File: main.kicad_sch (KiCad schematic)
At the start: 84 parts, among them J1 USB_C_Receptacle, J2 Bus_M.2_Socket_M, U2 SPI_SOIC-8, U3 SPI_DFN-8, Y1 25MHz

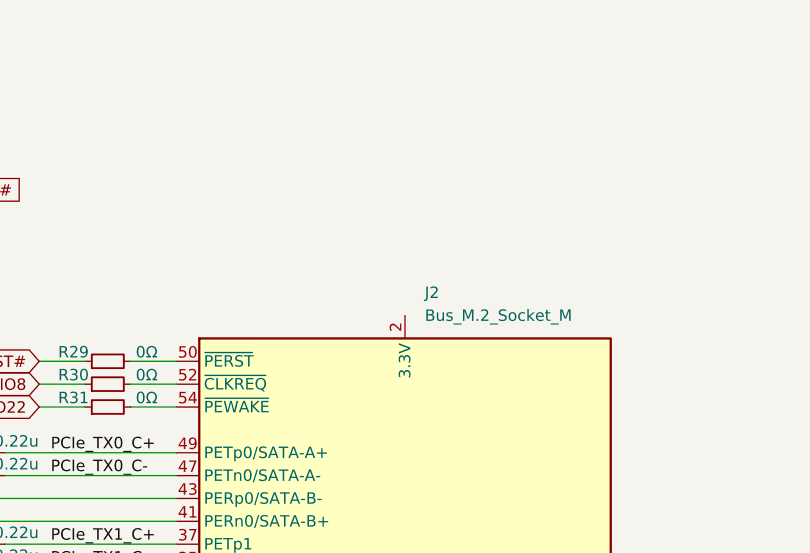
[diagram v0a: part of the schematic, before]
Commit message: Updated power rails
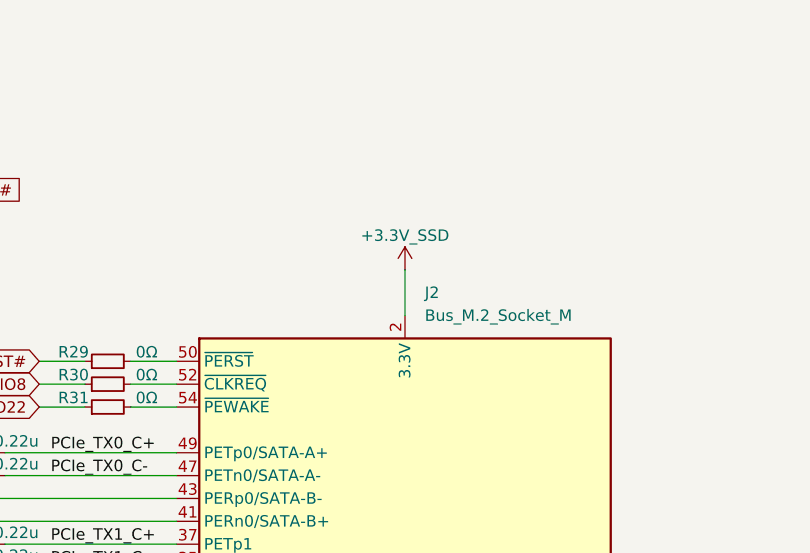
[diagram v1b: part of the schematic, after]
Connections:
- net +3.3V_SSD: now reaches J2.12 (3.3V), J2.14 (3.3V), J2.16 (3.3V), J2.18 (3.3V), J2.2 (3.3V), J2.4 (3.3V), J2.70 (3.3V), J2.72 (3.3V), J2.74 (3.3V)
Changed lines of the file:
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@@
 	(wire
 		(pts
+			(xy 481.33 55.88) (xy 481.33 60.96)
+		)
+		(stroke
+			(width 0)
+			(type default)
+		)
+	)
+	(wire
+		(pts
 			(xy 217.17 167.64) (xy 217.17 170.18)
 		)
@@
 				)
 			)
+		)
+	)
+	(symbol
+		(lib_id "power:+3.3V")
+		(at 481.33 55.88 0)
+		(unit 1)
+		(exclude_from_sim no)
+		(in_bom yes)
+		(on_board yes)
+		(dnp no)
+		(property "Reference" "#PWR041"
+			(at 481.33 59.69 0)
+			(effects
+				(font
+					(size 1.27 1.27)
+				)
+				(hide yes)
+			)
+		)
+		(property "Value" "+3.3V_SSD"
+			(at 481.33 52.07 0)
+			(effects
+				(font
+					(size 1.27 1.27)
+				)
+			)
+		)
+		(property "Footprint" ""
+			(at 481.33 55.88 0)
+			(effects
+				(font
+					(size 1.27 1.27)
+				)
+				(hide yes)
+			)
+		)
+		(property "Datasheet" ""
+			(at 481.33 55.88 0)
+			(effects
+				(font
+					(size 1.27 1.27)
+				)
+				(hide yes)
+			)
+		)
+		(property "Description" "Power symbol creates a global label with name \"+3.3V\""
+			(at 481.33 55.88 0)
+			(effects
+				(font
+					(size 1.27 1.27)
+				)
+				(hide yes)
+			)
+		)
+		(pin "1"
+		)
+		(instances
+			(project "ASM2464PD-test"
+				(path "/b2a945ac-f788-482b-9831-47d865c602eb/12c26485-ec0e-483e-81eb-3c9eea5d2424"
+					(reference "#PWR041")
+					(unit 1)
+				)
+			)

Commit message: Added todo list
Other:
- note added: "TODO: [ ] UART header 3V3 GND TX RX [ ] I2C header 3V3 GND CLK DATA [ ] SPI header with SPI flash pinout [ ] Jumper/button for SPI /HOLD [ ] Jumper/button for ASM RST#"
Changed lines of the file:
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@@
+		)
+	)
+	(text "TODO:\n[ ] UART header 3V3 GND TX RX\n[ ] I2C header 3V3 GND CLK DATA\n[ ] SPI header with SPI flash pinout\n[ ] Jumper/button for SPI /HOLD\n[ ] Jumper/button for ASM RST#"
+		(exclude_from_sim no)
+		(at 411.48 278.13 0)
+		(effects
+			(font
+				(size 1.27 1.27)
+			)
+			(justify left)
 		)
 	)

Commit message: Changing from M.2 adapter to PCIe x4 adapter
I don't actually want an ssd enclosure, I want a PCIe-slot-giver for my laptop
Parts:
- removed J2: Bus_M.2_Socket_M, A_my_stuff:m-key, symbol Connector:Bus_M.2_Socket_M
- removed R29: 0Ω, Resistor_SMD:R_0201_0603Metric, symbol Device:R_Small
- added J3: Bus_PCI_Express_x4, A-my-stuff:PCIe_x4_tht_open, symbol Connector:Bus_PCI_Express_x4
- C10, C11, C20, C21: footprint Capacitor_SMD:C_0201_0603Metric -> Capacitor_SMD:C_0402_1005Metric
- D1, D2: footprint (none) -> LED_SMD:LED_0603_1608Metric
- TP1, TP10, TP11, TP2, TP3, TP4, TP5, TP6, TP7, TP8, TP9: footprint (none) -> TestPoint:TestPoint_Pad_D2.0mm
- U1: footprint A_my_stuff:ASM2464PD -> A-my-stuff:ASM2464PD
- U2: footprint Package_SO:SOIC-8_5.23x5.23mm_P1.27mm -> Package_SO:SOIC-8_5.3x5.3mm_P1.27mm
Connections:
- net +3.3V_SSD: now also J3.A10 (+3.3V), J3.A9 (+3.3V), J3.B10 (3.3Vaux), J3.B8 (+3.3V)
- net GND: now also J3.A1 (~{PRSNT1}), J3.A12 (GND), J3.A15 (GND), J3.A18 (GND), J3.A20 (GND), J3.A23 (GND), J3.A24 (GND), J3.A27 (GND), J3.A28 (GND), J3.A31 (GND), J3.A4 (GND), J3.B13 (GND), J3.B16 (GND), J3.B18 (GND), J3.B21 (GND), J3.B22 (GND), J3.B25 (GND), J3.B26 (GND), J3.B29 (GND), J3.B32 (GND), J3.B4 (GND), J3.B7 (GND)
- net PCIe_RX0+: now also J3.A16 (PERp0)
- net PCIe_RX0-: now also J3.A17 (PERn0)
- net PCIe_RX1+: now also J3.A21 (PERp1)
- net PCIe_RX1-: now also J3.A22 (PERn1)
- net PCIe_RX2+: now also J3.A25 (PERp2)
- net PCIe_RX2-: now also J3.A26 (PERn2)
- net PCIe_RX3+: now also J3.A29 (PERp3)
- net PCIe_RX3-: now also J3.A30 (PERn3)
- net PCIe_TX0_C+: now also J3.B14 (PETp0)
- net PCIe_TX0_C-: now also J3.B15 (PETn0)
- net PCIe_TX1_C+: now also J3.B19 (PETp1)
- net PCIe_TX1_C-: now also J3.B20 (PETn1)
- net PCIe_TX2_C+: now also J3.B23 (PETp2)
- net PCIe_TX2_C-: now also J3.B24 (PETn2)
- net PCIe_TX3_C+: now also J3.B27 (PETp3)
- net PCIe_TX3_C-: now also J3.B28 (PETn3)
- net PERST#: now also J3.A11 (~{PERST})
- net REFCLK+: now also J3.A13 (REFCLK+)
- net REFCLK-: now also J3.A14 (REFCLK-)
- net at R31.2: now also J3.B11 (~{WAKE})
- net at R30.2: now also J3.B17 (~{PRSNT2}), J3.B31 (~{PRSNT2})
- new net: J3.A2 (+12V), J3.A3 (+12V), J3.B1 (+12V), J3.B2 (+12V), J3.B3 (+12V)
- no-connect marks 2 -> 0
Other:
- moved on the sheet: C12, C13, C14, C15, C16, C17, C18, C19, R30, R31

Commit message: Cleaning up schematic a bit
Directly copying the reference schematic was stupid lol, what a mess
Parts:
- removed unit 6 of U1
- removed unit 3 of U1
- removed unit 4 of U1
- removed unit 5 of U1
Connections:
- net GND: now also C21.1, R36.1, R37.1, R38.1; no longer C21.2, R36.2, R37.2, R38.2
- net RST#: now also C21.2; no longer C21.1
- net SPI_DO: now also R37.2; no longer R37.1
- net TEST_EN: now also R38.2; no longer R38.1
- net UART_TX: now also R36.2; no longer R36.1
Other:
- note added: "TODO: [ ] UART header 3V3 GND TX RX [ ] I2C header 3V3 GND CLK DATA [ ] SPI header with SPI flash pinout [ ] Jumper/button for SPI /HOLD [ ] Jumper/button for ASM RST# [ ] CC testpoints"
- note removed: "TODO: [ ] UART header 3V3 GND TX RX [ ] I2C header 3V3 GND CLK DATA [ ] SPI header with SPI flash pinout [ ] Jumper/button for SPI /HOLD [ ] Jumper/button for ASM RST#"
- moved on the sheet: C1, C10, C11, C12, C13, C14, C15, C16, C17, C18, C19, C2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

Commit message: power notes
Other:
- title: (none) -> ASM2464PD USB, PCIe, SPI & GPIO
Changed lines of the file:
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@@
 	(generator_version "9.0")
 	(paper "A3")
+	(title_block
+		(title "ASM2464PD USB, PCIe, SPI & GPIO")
+	)
 	(rectangle
 		(start 67.31 209.55)

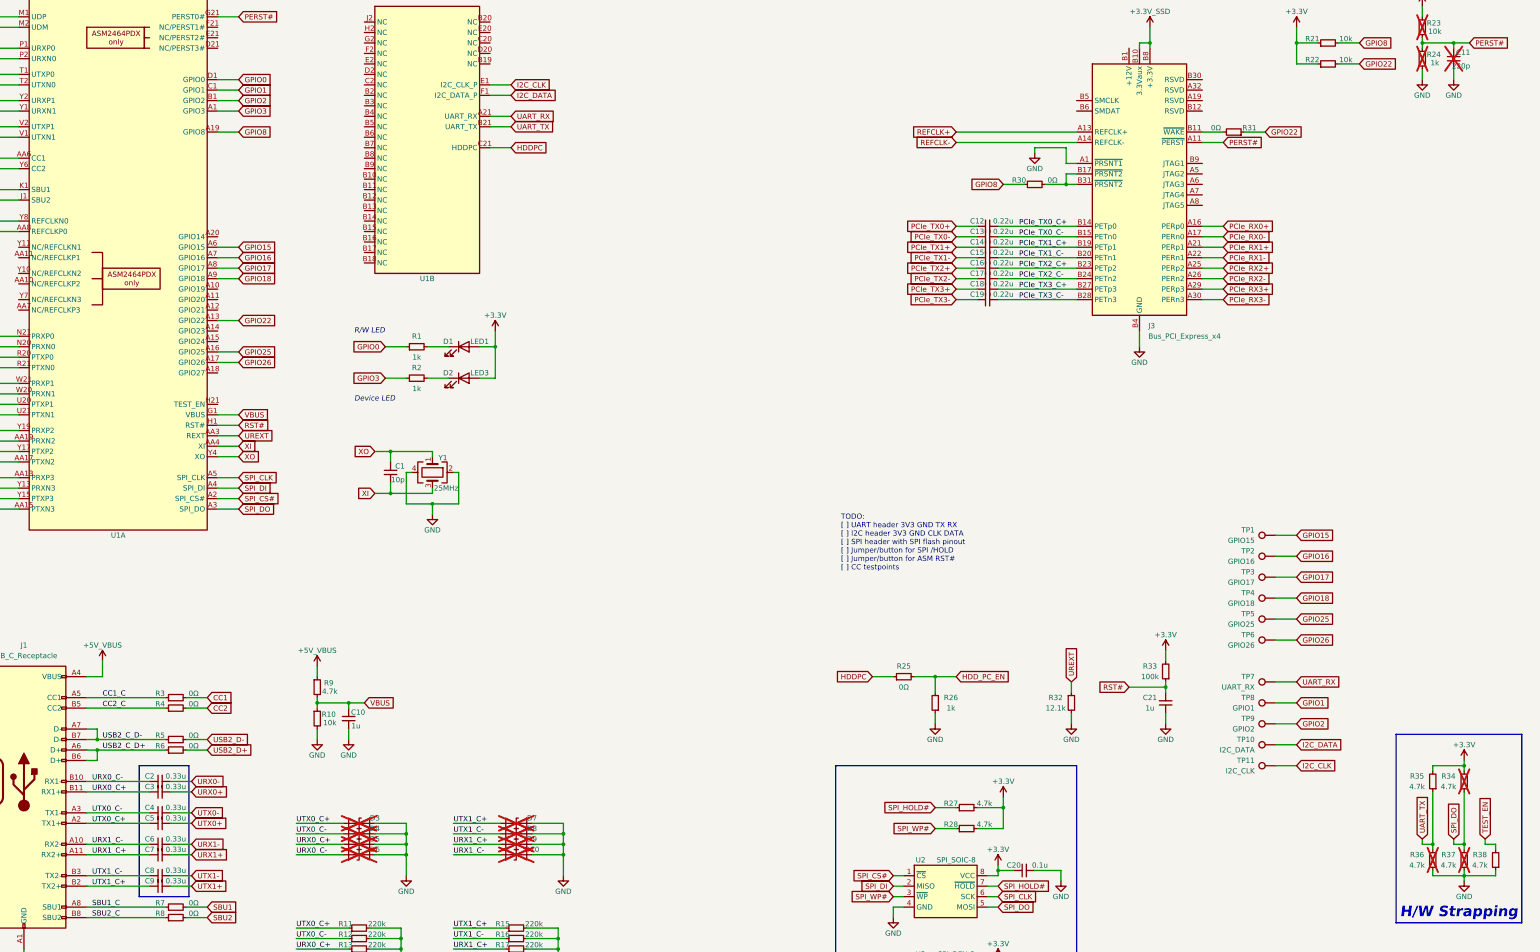
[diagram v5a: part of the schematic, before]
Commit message: Added function names to gpio pins
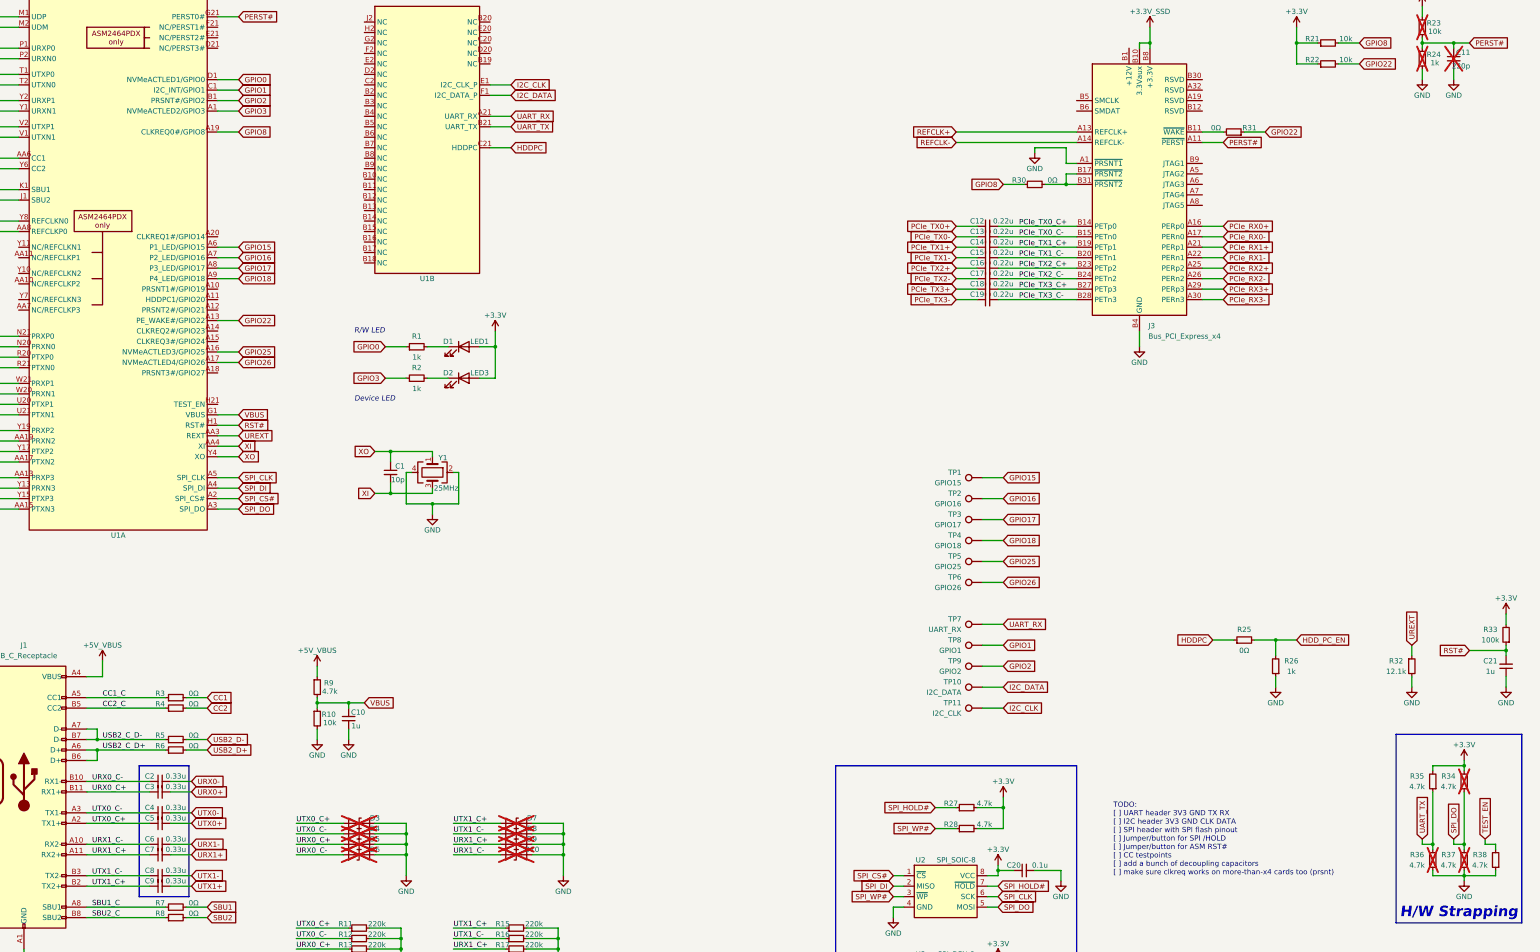
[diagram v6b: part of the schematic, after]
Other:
- note added: "TODO: [ ] UART header 3V3 GND TX RX [ ] I2C header 3V3 GND CLK DATA [ ] SPI header with SPI flash pinout [ ] Jumper/button for SPI /HOLD [ ] Jumper/button for ASM RST# [ ] CC testpoints [ ] add a bunch of decoupling capacitors [ ] make sure clkreq works on more-than-x4 cards too (prsnt)"
- note removed: "TODO: [ ] UART header 3V3 GND TX RX [ ] I2C header 3V3 GND CLK DATA [ ] SPI header with SPI flash pinout [ ] Jumper/button for SPI /HOLD [ ] Jumper/button for ASM RST# [ ] CC testpoints"
- moved on the sheet: C21, R25, R26, R32, R33, TP1, TP10, TP11, TP2, TP3, TP4, TP5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

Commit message: more pin names, more schematic cleanup, added SPI header
baby I don't know when I'm supposed to stop (I should go to bed)
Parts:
- removed TP1: GPIO15, TestPoint:TestPoint_Pad_D2.0mm, symbol Connector:TestPoint
- removed TP10: I2C_DATA, TestPoint:TestPoint_Pad_D2.0mm, symbol Connector:TestPoint
- removed TP11: I2C_CLK, TestPoint:TestPoint_Pad_D2.0mm, symbol Connector:TestPoint
- removed TP2: GPIO16, TestPoint:TestPoint_Pad_D2.0mm, symbol Connector:TestPoint
- removed TP3: GPIO17, TestPoint:TestPoint_Pad_D2.0mm, symbol Connector:TestPoint
- removed TP4: GPIO18, TestPoint:TestPoint_Pad_D2.0mm, symbol Connector:TestPoint
- removed TP5: GPIO25, TestPoint:TestPoint_Pad_D2.0mm, symbol Connector:TestPoint
- removed TP6: GPIO26, TestPoint:TestPoint_Pad_D2.0mm, symbol Connector:TestPoint
- removed TP7: UART_RX, TestPoint:TestPoint_Pad_D2.0mm, symbol Connector:TestPoint
- removed TP8: GPIO1, TestPoint:TestPoint_Pad_D2.0mm, symbol Connector:TestPoint
- removed TP9: GPIO2, TestPoint:TestPoint_Pad_D2.0mm, symbol Connector:TestPoint
- added D11, D12, D13, D14, D15, D16: ~, LED_SMD:LED_0603_1608Metric, symbol Device:LED
- added J2: SPIheader, Connector_PinHeader_2.54mm:PinHeader_2x04_P2.54mm_Vertical, symbol Connector_Generic:Conn_02x04_Odd_Even
- added R20, R29, R39, R41, R42, R43: 1k, Resistor_SMD:R_0402_1005Metric, symbol Device:R_Small
- C1: footprint Capacitor_SMD:C_0201_0603Metric -> Capacitor_SMD:C_0402_1005Metric
- D1: value LED1 -> ~
- D2: value LED3 -> ~
- R10, R2, R21, R22, R23, R24, R25, R26, R27, R28, R3, R30, R31, R32, R33, R34, R35, R36, R37, R38, R4, R5, R6, R7, R8, R9: footprint Resistor_SMD:R_0201_0603Metric -> Resistor_SMD:R_0402_1005Metric
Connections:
- net GND: now also J2.7 (Pin_7)
- net SPI_CLK: now also J2.6 (Pin_6)
- net SPI_CS#: now also J2.1 (Pin_1)
- net SPI_DI: now also J2.3 (Pin_3)
- net SPI_DO: now also J2.8 (Pin_8)
- net SPI_HOLD#: now also J2.4 (Pin_4)
- net SPI_WP#: now also J2.5 (Pin_5)
- net GPIO19: now reaches U1.A10 (PRSNT1#/GPIO19)
- net GPIO20: now reaches U1.A11 (HDDPC1/GPIO20)
- net GPIO21: now reaches U1.A12 (PRSNT2#/GPIO21)
- net CLKREQ2#: now reaches U1.A14 (CLKREQ2#/GPIO23)
- net CLKREQ3#: now reaches U1.A15 (CLKREQ3#/GPIO24)
- net GPIO27: now reaches U1.A18 (PRSNT3#/GPIO27)
- net CLKREQ1#: now reaches U1.A20 (CLKREQ1#/GPIO14)
- net +3.3V renamed +3.3V_LDO
- net +3.3V_LDO: now also D11.2 (A), D12.2 (A), D13.2 (A), D14.2 (A), D15.2 (A), D16.2 (A), J2.2 (Pin_2)
- net GPIO0 renamed ActLED1
- net GPIO15 renamed P1_LED
- net P1_LED: now also R39.1
- net GPIO16 renamed P2_LED
- net P2_LED: now also R41.1
- net GPIO17 renamed P3_LED
- net P3_LED: now also R42.1
- net GPIO18 renamed P4_LED
- net P4_LED: now also R43.1
- net GPIO22 renamed PE_WAKE#
- net GPIO25 renamed ActLED3
- net ActLED3: now also R20.1
- net GPIO26 renamed ActLED4
- net ActLED4: now also R29.1
- net GPIO3 renamed ActLED2
- net GPIO8 renamed CLKREQ0#
- net PERST# renamed PERST0#
- new net: D11.1 (K), R20.2
- new net: D13.1 (K), R39.2
- new net: D14.1 (K), R41.2
- new net: D15.1 (K), R42.2
- new net: D16.1 (K), R43.2
- new net: D12.1 (K), R29.2
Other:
- note added: "Mystery LED"
- note added: "Mystery LED 2"
- note added: "Ultra-Mystery LED"
- note added: "Ultra-Mystery LED 2"
- note added: "Ultra-Mystery LED 3"
- note added: "Ultra-Mystery LED 4"
- moved on the sheet: D1, D2, R1, R2, R21, R22
